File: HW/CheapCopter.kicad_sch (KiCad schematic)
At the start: 17 parts, among them M5 3-5V, M6 3-5V, M7 3-5V, M8 3-5V, U1 ESP32-WROOM-32, U2 MPU-6050, U3 L293D, U4 L293D, U5 ESP32-WROOM-32, U6 L7805

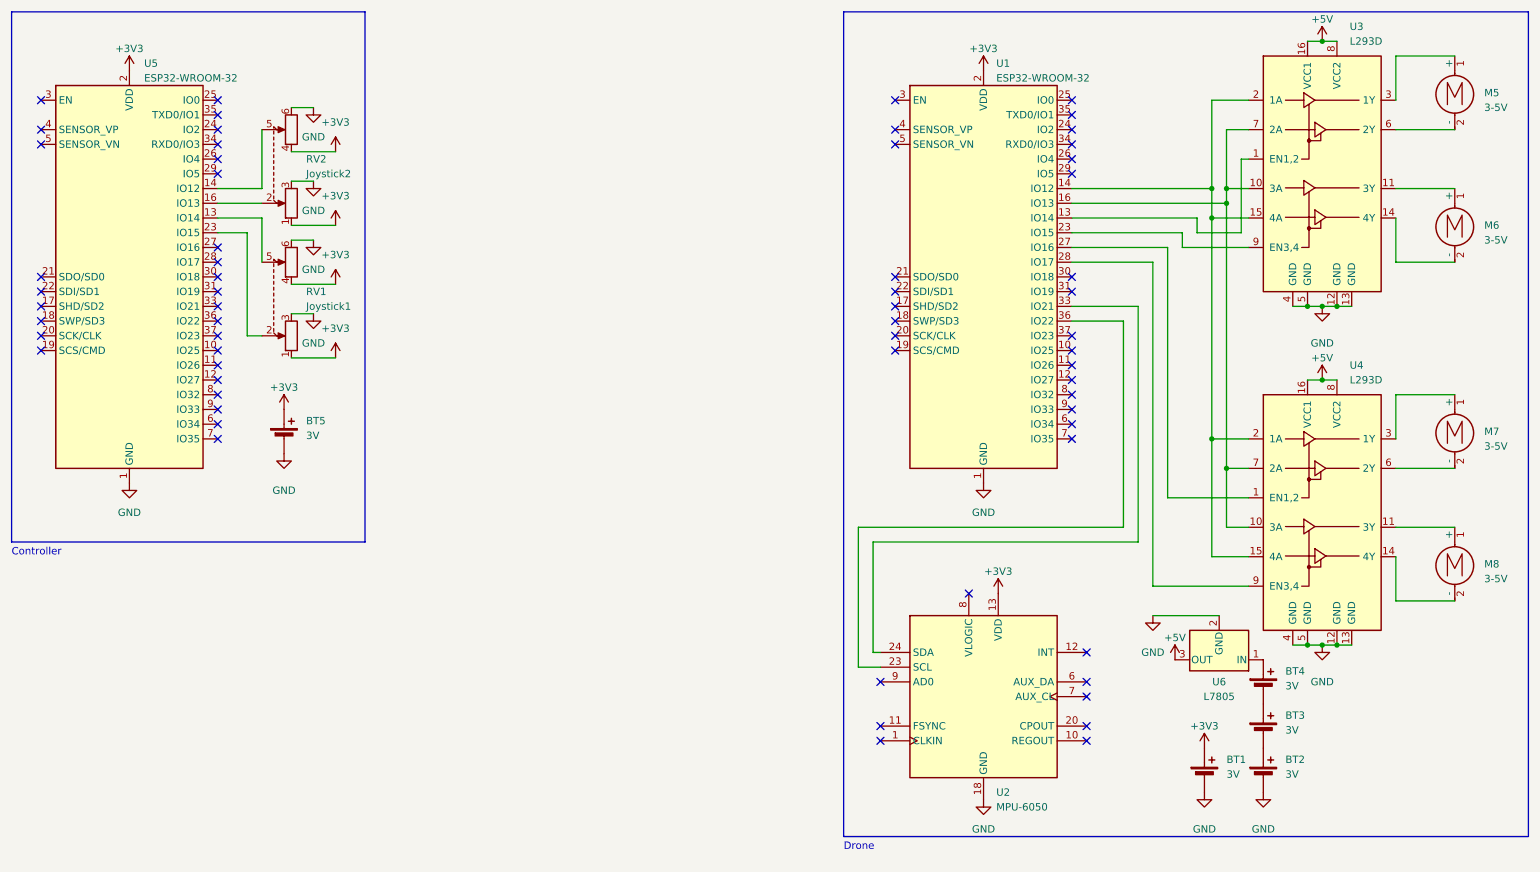
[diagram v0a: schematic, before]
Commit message: First code
Added code for WiFi AP, OTA and basic wireless controlling
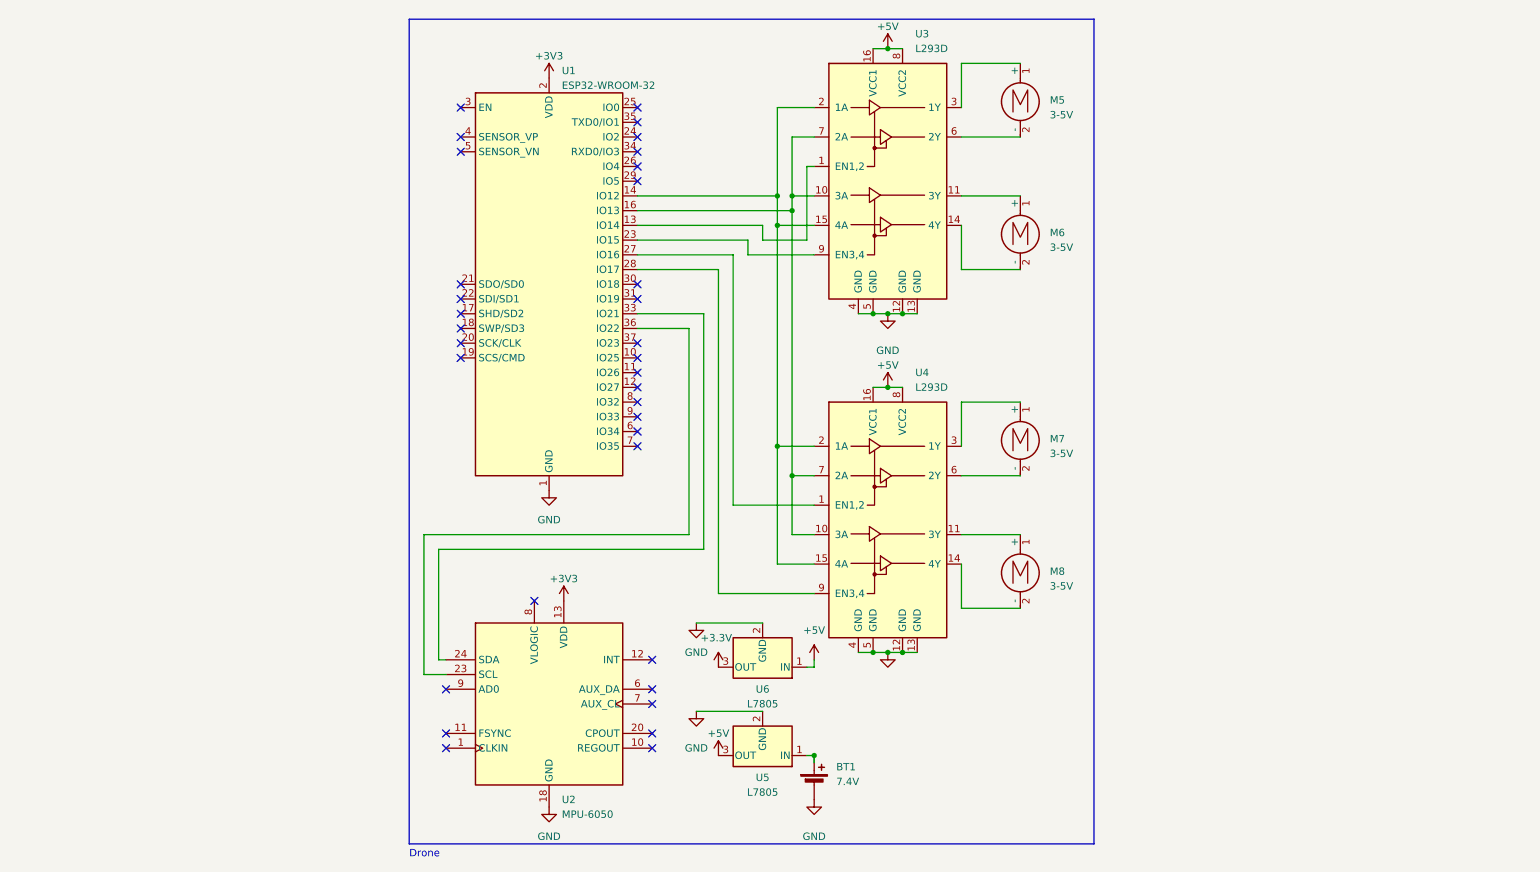
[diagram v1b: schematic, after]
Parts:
- removed BT2, BT3, BT4: 3V, Battery:BatteryHolder_Keystone_103_1x20mm, symbol Device:Battery_Cell
- removed BT5: 3V, symbol Device:Battery_Cell
- removed RV1: Joystick1, symbol Device:R_Potentiometer_Dual
- removed RV2: Joystick2, symbol Device:R_Potentiometer_Dual
- removed U5: ESP32-WROOM-32, RF_Module:ESP32-WROOM-32, symbol RF_Module:ESP32-WROOM-32
- added U6: L7805, Transformer_THT:TO255P1020X450X2000-3, symbol Regulator_Linear:L7805
- BT1: value 3V -> 7.4V
- renumbered U6 to U5
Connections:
- net +3V3: no longer BT1.1 (+)
- net +5V: now also U6.1 (IN)
- net GND: now also U6.2 (GND)
- net at U5.1 (IN): now also BT1.1 (+)
- new net +3.3V: U6.3 (OUT)
- no-connect marks 63 -> 34
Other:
- note removed: "Controller"
- moved on the sheet: BT1, M5, M6, M7, M8, U1, U2, U3, U4, U5
